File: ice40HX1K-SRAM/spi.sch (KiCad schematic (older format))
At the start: 9 parts

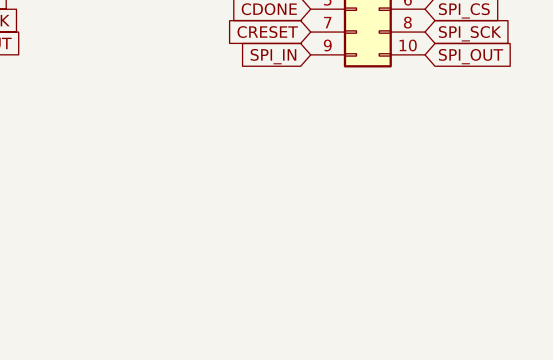
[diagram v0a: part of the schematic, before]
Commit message: add ASE-10.000MHZ XTAL
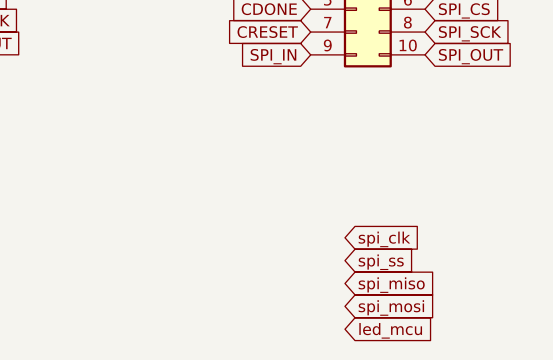
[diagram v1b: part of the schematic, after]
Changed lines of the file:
@@
 $Descr A4 11693 8268
 encoding utf-8
-Sheet 3 8
+Sheet 3 9
 Title ""
 Date ""
@@
 NoConn ~ 7900 2100
 NoConn ~ 7400 2100
+Text GLabel 7550 3200 2    50   Input ~ 0
+spi_clk
+Text GLabel 7550 3300 2    50   Input ~ 0
+spi_ss
+Text GLabel 7550 3400 2    50   Input ~ 0
+spi_miso
+Text GLabel 7550 3500 2    50   Input ~ 0
+spi_mosi
+Text GLabel 7550 3600 2    50   Input ~ 0
+led_mcu
 $EndSCHEMATC
